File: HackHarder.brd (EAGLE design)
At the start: 67 x 80.1 mm, 8 parts, among them U1 RFM69HW

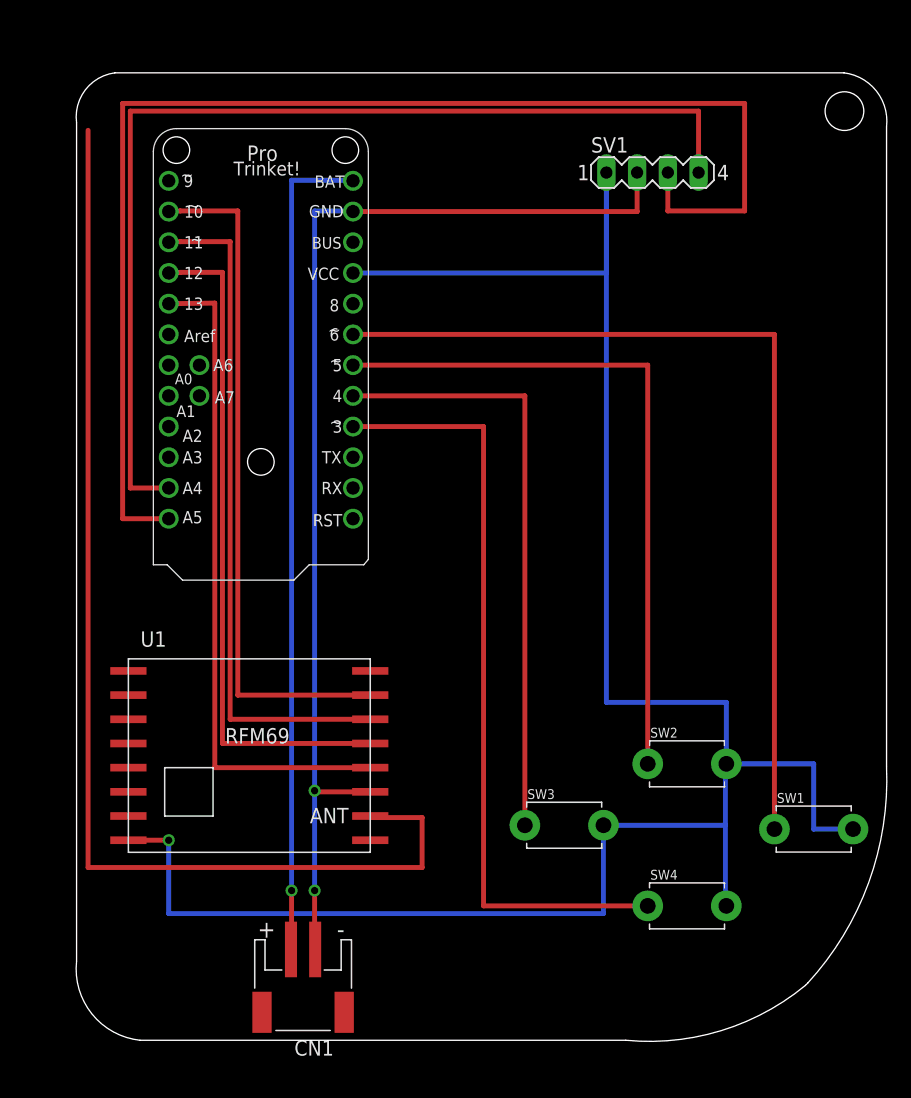
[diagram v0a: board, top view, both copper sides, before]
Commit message: Add files via upload
Updated board with smaller footprint
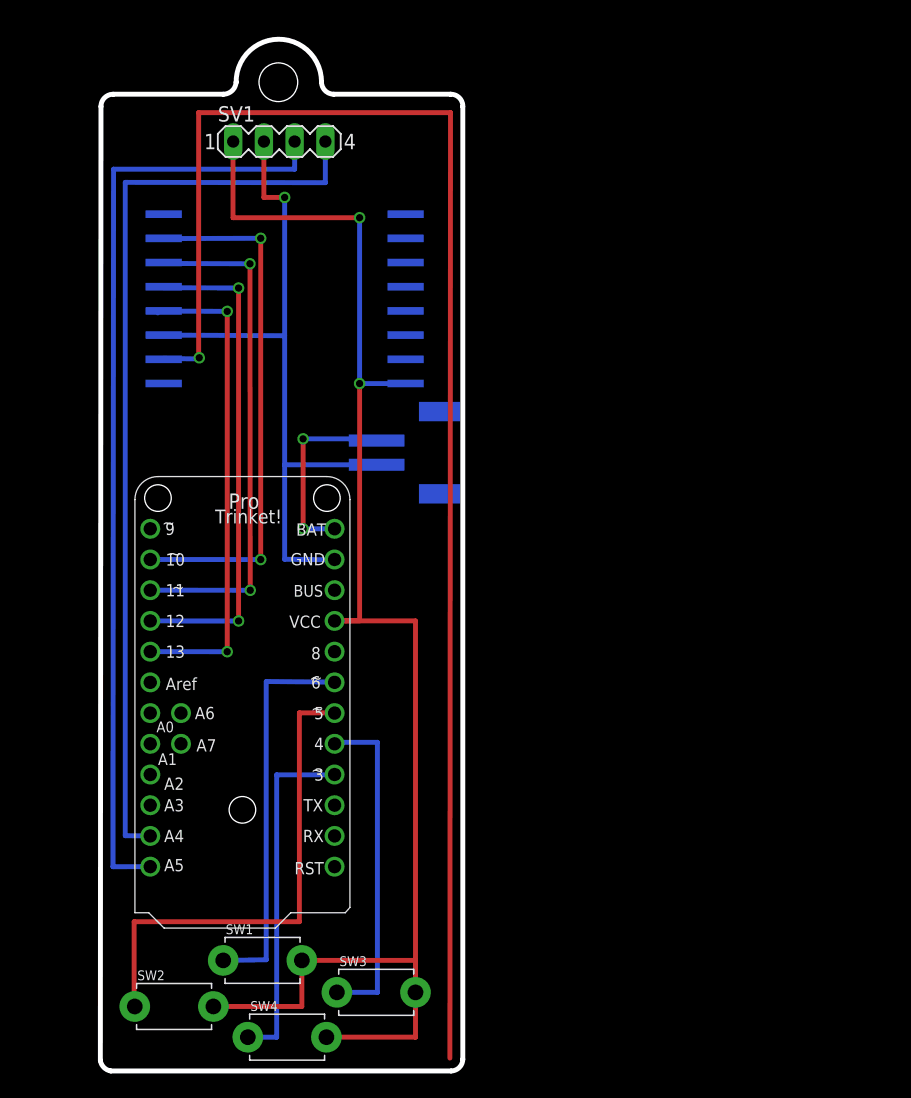
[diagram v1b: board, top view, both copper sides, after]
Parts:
- moved SW2 46.9 mm to (17.3, 2.79)
- moved SW1 46.9 mm to (24.6, 6.60)
- moved CN1 45.8 mm to (37.7, 48.6), flipped to the bottom, turned to 90 degrees
- moved U1 37.9 mm to (26.4, 60.3), flipped to the bottom
- moved SW4 34.8 mm to (26.6, 0.25)
- moved SV1 31.0 mm to (26.0, 74.3)
- moved MCU1 28.8 mm to (22.9, 19.1)
- moved SW3 20.8 mm to (34.0, 3.96)
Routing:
- net N$9: track 0.00 -> 122.3 mm
- net N$14 (its old number): track 96.8 -> 0.00 mm
- net N$2: track 68.8 -> 16.3 mm, vias 1 -> 2
- net VCC: track 179.2 -> 127.7 mm, vias 1 -> 2
- net N$12: track 75.8 -> 32.2 mm
- net G$1: track 95.8 -> 58.0 mm, vias 2 -> 1
- net N$15: track 63.8 -> 28.9 mm
- net N$3: track 108.0 -> 78.0 mm
- net N$14: track 49.7 -> 27.7 mm
- net N$13: track 57.3 -> 40.9 mm
- net N$7: track 55.1 -> 39.9 mm, vias 0 -> 2
- net N$6: track 55.6 -> 41.1 mm, vias 0 -> 2
- net N$5: track 56.2 -> 42.5 mm, vias 0 -> 2
- net N$8: track 56.7 -> 43.7 mm, vias 0 -> 2
- net N$4: track 86.4 -> 76.0 mm
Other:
- board size 67 x 80.1 mm -> 30 x 85.3 mm

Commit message: Add files via upload
Latest version
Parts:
- moved CN1 37.3 mm to (39.9, 11.4)
- moved SW4 12.2 mm to (15.3, 4.61)
- moved SW1 10.7 mm to (35.1, 4.56)
- moved MCU1 10.0 mm to (15.6, 25.9), turned to 270 degrees
- moved SW2 9.74 mm to (25.4, 8.12)
- moved SW3 9.09 mm to (25.4, 0.99)
- moved U1 5.76 mm to (24.9, 54.8)
- moved SV1 1.00 mm to (25.0, 74.3)
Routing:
- net N$11: track 0.00 -> 188.9 mm
- net N$9: track 122.3 -> 0.00 mm
- net G$1: track 58.0 -> 120.0 mm
- net VCC: track 127.7 -> 186.7 mm, vias 2 -> 0
- net N$13: track 40.9 -> 11.6 mm
- net N$3: track 78.0 -> 56.2 mm
- net N$4: track 76.0 -> 59.5 mm
- net N$12: track 32.2 -> 20.9 mm
- net N$15: track 28.9 -> 20.2 mm
- net N$2: track 16.3 -> 8.52 mm, vias 2 -> 0
- net N$8: track 43.7 -> 48.7 mm, vias 2 -> 0
- net N$7: track 39.9 -> 35.0 mm, vias 2 -> 0
- net N$14: track 27.7 -> 30.0 mm
- net N$5: track 42.5 -> 44.1 mm, vias 2 -> 0
- net N$6: track 41.1 -> 39.6 mm, vias 2 -> 0
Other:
- board size 30 x 85.3 mm -> 38.1 x 86.4 mm

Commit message: Add files via upload
Now with serial breakout!  I'm not sure that the footprint for the radio is correct - need to double-check the pintout on the module spec sheet...
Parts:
- added SERIAL: (no value), adafruit:1X03
- renumbered SV1 to OLED
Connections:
- new net N$16: MCU1.TX, SERIAL.1
- new net N$17: MCU1.RX, SERIAL.2
- net G$1: now also SERIAL.3
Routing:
- net G$1: track 120.0 -> 160.8 mm
- net N$16: track 0.00 -> 16.4 mm
- net N$17: track 0.00 -> 11.4 mm
- net N$11: track 188.9 -> 183.7 mm
- net N$14: track 30.0 -> 27.8 mm
- net N$12: track 20.9 -> 19.4 mm
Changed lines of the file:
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@@
 <element name="U1" library="HopeRF-RFMxx" package="RFM69_PADS" value="RFM69HW" x="24.9" y="54.7511" rot="MR0"/>
 <element name="MCU1" library="adafruit" package="PROTRINKET" value="PRO_TRINKET" x="15.5975" y="25.869" rot="R270"/>
-<element name="SV1" library="con-lstb" package="MA04-1" value="" x="24.9715" y="74.3204">
+<element name="OLED" library="con-lstb" package="MA04-1" value="" x="24.9715" y="74.3204">
 <attribute name="OC_FARNELL" value="unknown" x="24.9715" y="74.3204" size="1.778" layer="27" display="off"/>
 <attribute name="MF" value="" x="24.9715" y="74.3204" size="1.778" layer="27" display="off"/>
@@
 <element name="SW3" library="adafruit" package="TACT_PANA-EVQ" value="" x="25.3916" y="0.9892"/>
 <element name="SW4" library="adafruit" package="TACT_PANA-EVQ" value="" x="15.2716" y="4.6084"/>
+<element name="SERIAL" library="adafruit" package="1X03" value="" x="8.6868" y="11.6332" rot="R90"/>
 </elements>
 <signals>
@@
 <contactref element="CN1" pad="2"/>
 <contactref element="MCU1" pad="GND"/>
-<contactref element="SV1" pad="2"/>
+<contactref element="OLED" pad="2"/>
 <contactref element="U1" pad="GND"/>
 <wire x1="36.1966" y1="10.3682" x2="31.9532" y2="10.3682" width="0.4064" layer="16"/>
@@
 <wire x1="9.144" y1="52.7511" x2="14.9" y2="52.7511" width="0.4064" layer="16"/>
 <via x="9.144" y="52.7511" extent="1-16" drill="0.6"/>
+<contactref element="SERIAL" pad="3"/>
+<wire x1="8.6868" y1="14.1732" x2="8.6868" y2="22.8092" width="0.4064" layer="1"/>
+<wire x1="8.6868" y1="22.8092" x2="36.2985" y2="22.8092" width="0.4064" layer="1"/>
+<wire x1="36.2985" y1="22.8092" x2="36.2985" y2="18.249" width="0.4064" layer="1"/>
 </signal>
 <signal name="VCC">
 <contactref element="MCU1" pad="VCC"/>
-<contactref element="SV1" pad="1"/>
-<contactref element="U1" pad="VCC"/>
+<contactref element="OLED" pad="1"/>
 <contactref element="SW1" pad="P$2"/>
 <contactref element="SW3" pad="P$2"/>
@@
 <wire x1="8.0264" y1="65.4304" x2="8.0264" y2="74.3204" width="0.4064" layer="16"/>
 <wire x1="8.0264" y1="74.3204" x2="21.1615" y2="74.3204" width="0.4064" layer="16"/>
-<wire x1="34.9" y1="48.7511" x2="38.6588" y2="48.7511" width="0.4064" layer="16"/>
 <wire x1="38.6588" y1="48.7511" x2="38.6588" y2="65.4304" width="0.4064" layer="16"/>
 <wire x1="38.6588" y1="65.4304" x2="8.0264" y2="65.4304" width="0.4064" layer="16"/>
@@
 <wire x1="18.5216" y1="4.6084" x2="18.5216" y2="4.572" width="0.4064" layer="1"/>
 <wire x1="18.5216" y1="4.572" x2="28.6416" y2="4.572" width="0.4064" layer="1"/>
+<contactref element="U1" pad="VCC"/>
+<wire x1="38.6588" y1="48.7511" x2="34.9" y2="48.7511" width="0.4064" layer="16"/>
 </signal>
 <signal name="N$1">
@@
 <signal name="N$3">
 <contactref element="MCU1" pad="A5"/>
-<contactref element="SV1" pad="3"/>
+<contactref element="OLED" pad="3"/>
 <wire x1="26.2415" y1="74.3204" x2="26.2415" y2="70.104" width="0.4064" layer="1"/>
 <wire x1="26.2415" y1="70.104" x2="10.8712" y2="70.104" width="0.4064" layer="1"/>
@@
 <signal name="N$4">
 <contactref element="MCU1" pad="A4"/>
-<contactref element="SV1" pad="4"/>
+<contactref element="OLED" pad="4"/>
 <wire x1="28.7815" y1="74.3204" x2="28.7815" y2="68.9864" width="0.4064" layer="1"/>
 <wire x1="28.7815" y1="68.9864" x2="11.7856" y2="68.9864" width="0.4064" layer="1"/>
@@
 <contactref element="MCU1" pad="6"/>
 <contactref element="SW1" pad="P$1"/>
-<wire x1="26.1385" y1="18.249" x2="26.1385" y2="11.6332" width="0.4064" layer="16"/>
-<wire x1="26.1385" y1="11.6332" x2="25.4" y2="11.6332" width="0.4064" layer="16"/>
-<wire x1="25.4" y1="11.6332" x2="25.4" y2="4.56" width="0.4064" layer="16"/>
-<wire x1="25.4" y1="4.56" x2="31.8372" y2="4.56" width="0.4064" layer="16"/>
+<wire x1="31.8372" y1="4.56" x2="26.1385" y2="4.56" width="0.4064" layer="16"/>
+<wire x1="26.1385" y1="4.56" x2="26.1385" y2="18.249" width="0.4064" layer="16"/>
 </signal>
 <signal name="N$13">
 <contactref element="MCU1" pad="5"/>
 <contactref element="SW2" pad="P$1"/>
-<wire x1="23.5985" y1="18.249" x2="23.5985" y2="12.192" width="0.4064" layer="16"/>
-<wire x1="23.5985" y1="12.192" x2="22.1488" y2="12.192" width="0.4064" layer="16"/>
-<wire x1="22.1488" y1="12.192" x2="22.1488" y2="8.1244" width="0.4064" layer="16"/>
-<wire x1="22.1488" y1="8.1244" x2="22.1744" y2="8.1244" width="0.4064" layer="16"/>
+<wire x1="23.5985" y1="18.249" x2="23.5985" y2="8.1244" width="0.4064" layer="16"/>
+<wire x1="23.5985" y1="8.1244" x2="22.1744" y2="8.1244" width="0.4064" layer="16"/>
 </signal>
 <signal name="N$14">
 <contactref element="MCU1" pad="4"/>
 <contactref element="SW3" pad="P$1"/>
-<wire x1="21.0585" y1="18.249" x2="21.0585" y2="13.208" width="0.4064" layer="16"/>
-<wire x1="21.0585" y1="13.208" x2="15.24" y2="13.208" width="0.4064" layer="16"/>
-<wire x1="15.24" y1="13.208" x2="15.24" y2="0.9892" width="0.4064" layer="16"/>
-<wire x1="15.24" y1="0.9892" x2="22.1416" y2="0.9892" width="0.4064" layer="16"/>
+<wire x1="21.0585" y1="18.249" x2="21.0585" y2="10.6172" width="0.4064" layer="16"/>
+<wire x1="21.0585" y1="10.6172" x2="16.3068" y2="10.6172" width="0.4064" layer="16"/>
+<wire x1="16.3068" y1="10.6172" x2="16.3068" y2="0.9892" width="0.4064" layer="16"/>
+<wire x1="16.3068" y1="0.9892" x2="22.1416" y2="0.9892" width="0.4064" layer="16"/>
 </signal>
 <signal name="N$15">
 <contactref element="MCU1" pad="3"/>
 <contactref element="SW4" pad="P$1"/>
-<wire x1="18.5185" y1="18.249" x2="18.5185" y2="14.1732" width="0.4064" layer="16"/>
-<wire x1="18.5185" y1="14.1732" x2="11.9888" y2="14.1732" width="0.4064" layer="16"/>
-<wire x1="11.9888" y1="14.1732" x2="11.9888" y2="4.6084" width="0.4064" layer="16"/>
-<wire x1="11.9888" y1="4.6084" x2="12.0216" y2="4.6084" width="0.4064" layer="16"/>
+<wire x1="18.5185" y1="18.249" x2="18.5185" y2="11.6332" width="0.4064" layer="16"/>
+<wire x1="18.5185" y1="11.6332" x2="15.24" y2="11.6332" width="0.4064" layer="16"/>
+<wire x1="15.24" y1="11.6332" x2="15.24" y2="4.6084" width="0.4064" layer="16"/>
+<wire x1="15.24" y1="4.6084" x2="12.0216" y2="4.6084" width="0.4064" layer="16"/>
 </signal>
 <signal name="N$11">
-<wire x1="14.986" y1="50.8" x2="20.32" y2="50.8" width="0.4064" layer="16"/>
-<wire x1="20.32" y1="50.8" x2="20.32" y2="44.704" width="0.4064" layer="16"/>
-<wire x1="20.32" y1="44.704" x2="41.656" y2="44.704" width="0.4064" layer="1"/>
-<wire x1="41.656" y1="44.704" x2="41.656" y2="82.3468" width="0.4064" layer="1"/>
-<wire x1="41.656" y1="82.3468" x2="6.604" y2="82.3468" width="0.4064" layer="1"/>
-<wire x1="6.604" y1="82.3468" x2="6.604" y2="-1.1176" width="0.4064" layer="1"/>
-<via x="20.32" y="44.704" extent="1-16" drill="0.6"/>
+<wire x1="14.986" y1="50.8" x2="25.654" y2="50.8" width="0.4064" layer="16"/>
+<wire x1="25.654" y1="50.8" x2="25.654" y2="44.704" width="0.4064" layer="16"/>
+<wire x1="25.654" y1="44.704" x2="41.656" y2="44.704" width="0.4064" layer="1"/>
+<wire x1="41.656" y1="44.704" x2="41.656" y2="82.296" width="0.4064" layer="1"/>
+<wire x1="41.656" y1="82.296" x2="6.604" y2="82.296" width="0.4064" layer="1"/>
+<wire x1="6.604" y1="82.296" x2="6.604" y2="4.0132" width="0.4064" layer="1"/>
+<via x="25.654" y="44.704" extent="1-16" drill="0.6"/>
+</signal>
+<signal name="N$16">
+<contactref element="MCU1" pad="TX"/>
+<contactref element="SERIAL" pad="1"/>
+<wire x1="8.6868" y1="9.0932" x2="14.3256" y2="9.0932" width="0.4064" layer="16"/>
+<wire x1="14.3256" y1="9.0932" x2="14.3256" y2="12.7" width="0.4064" layer="16"/>
+<wire x1="14.3256" y1="12.7" x2="15.9785" y2="12.7" width="0.4064" layer="16"/>
+<wire x1="15.9785" y1="12.7" x2="15.9785" y2="18.249" width="0.4064" layer="16"/>
+</signal>
+<signal name="N$17">
+<contactref element="MCU1" pad="RX"/>
+<contactref element="SERIAL" pad="2"/>
+<wire x1="8.6868" y1="11.6332" x2="13.4385" y2="11.6332" width="0.4064" layer="16"/>
+<wire x1="13.4385" y1="11.6332" x2="13.4385" y2="18.249" width="0.4064" layer="16"/>
 </signal>
 </signals>
